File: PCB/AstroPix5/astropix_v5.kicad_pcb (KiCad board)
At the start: 4 copper layers, 56.4 x 65.5 mm, 39 parts, among them J1 HBOut, J12 Measures_Analog, J13 pcie_GECCO, J14 Bias, J2 Conn_01x05, J4 HBOut, J5 HBOut, J7 HV_in_external, J8 Conn_01x03, U2 AstroPix5_split_powerring

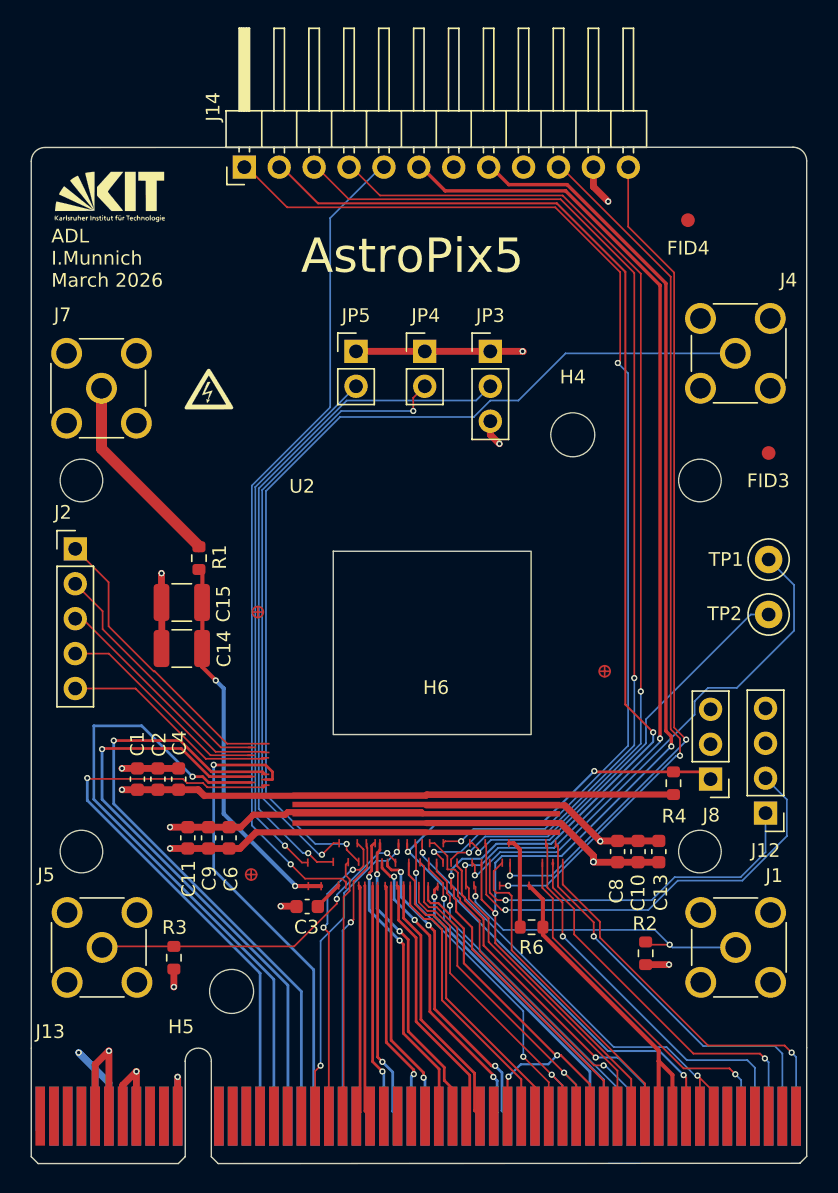
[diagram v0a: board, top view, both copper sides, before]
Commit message: Gecco schematic changes and new fan out layout routing
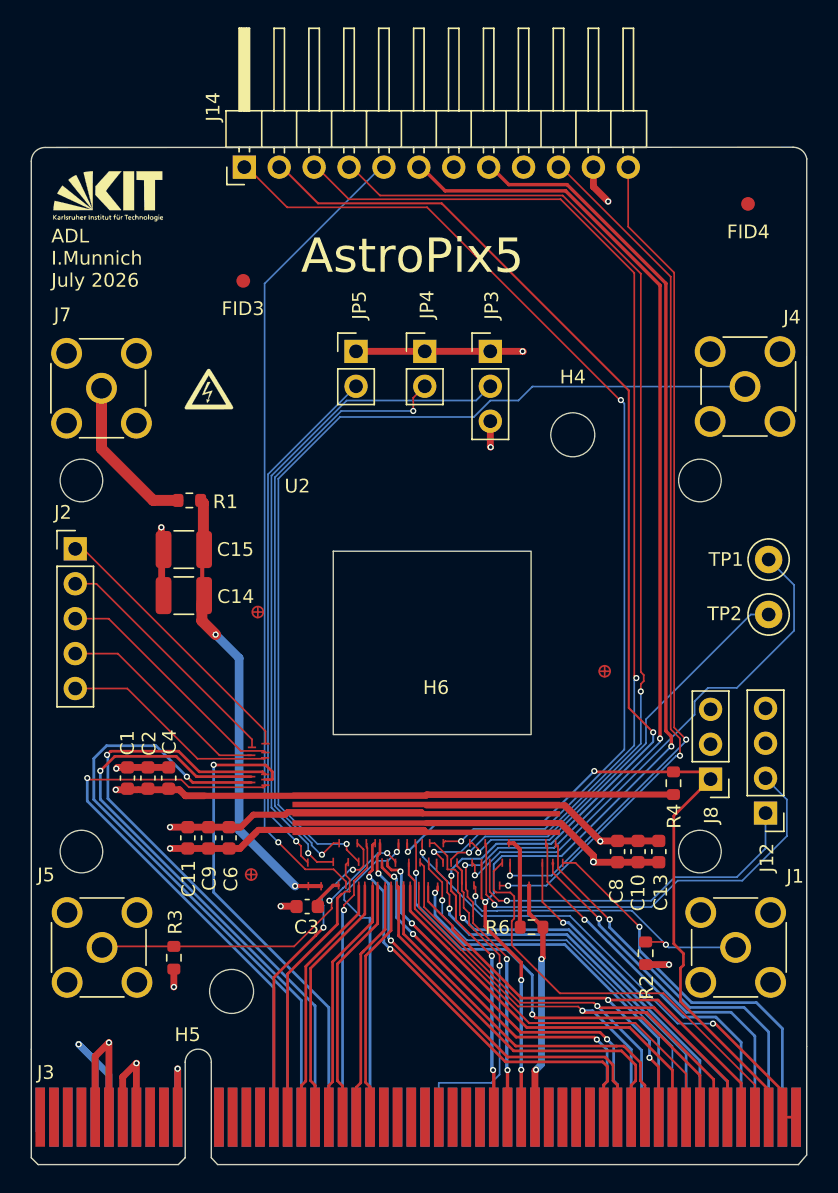
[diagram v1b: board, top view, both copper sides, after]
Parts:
- removed J13: pcie_GECCO, Connector_PCBEdge:BUS_PCIexpress_x16
- added J3: pcie_GECCO, Connector_PCBEdge:BUS_PCIexpress_x16_ilo, F.Cu at (156.0, 130.6)
- moved FID3 40.2 mm to (170.8, 69.7)
- moved FID4 4.53 mm to (207.5, 64.1)
- moved R1 4.26 mm to (166.8, 85.7), turned to 0 degrees
- moved C14 3.85 mm to (166.4, 92.6)
- moved C15 3.85 mm to (166.4, 89.3)
- moved J4 2.52 mm to (207.3, 77.4)
- moved C1 0.73 mm to (162.3, 105.9)
- moved C2 0.73 mm to (163.8, 105.9)
- moved C4 0.73 mm to (165.3, 105.9)
- moved Logo4 0.13 mm to (160.9, 63.6)
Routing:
- net /SR_ck1: track 24.7 -> 40.6 mm
- net /SR_ck2: track 27.0 -> 42.8 mm
- net /SR_sin: track 29.2 -> 42.0 mm
- net /hold: track 23.9 -> 35.0 mm
- net /Clk20_Ext_P: track 19.1 -> 28.8 mm
- net /Clk20_Ext_N: track 19.1 -> 28.7 mm
- net /SPI_MISO0_P: track 22.1 -> 31.6 mm
- net /SPI_MISO0_N: track 22.2 -> 31.4 mm
- net /res_n: track 22.6 -> 31.4 mm
- net /syncres: track 20.4 -> 29.1 mm
- net /blpix: track 104.6 -> 96.4 mm, vias 2 -> 4
- net /DigInj: track 23.8 -> 31.8 mm
- net /vminuspix: track 25.1 -> 17.5 mm, vias 0 -> 2
- net /SPI_CLK_P: track 22.2 -> 28.9 mm
- net /SPI_CLK_N: track 22.5 -> 29.1 mm
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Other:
- board size 56.4 x 65.5 mm -> 56.4 x 65.6 mm
- board text added: "ADL I.Munnich July 2026"
- board text removed: "ADL I.Munnich March 2026"
